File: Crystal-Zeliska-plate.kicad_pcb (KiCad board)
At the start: 2 copper layers, 182.6 x 114.3 mm, 0 parts

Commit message: updated Gerber
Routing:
- net (no net): track 0.00 -> 19.8 mm
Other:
- outline, holes or cut-outs redrawn

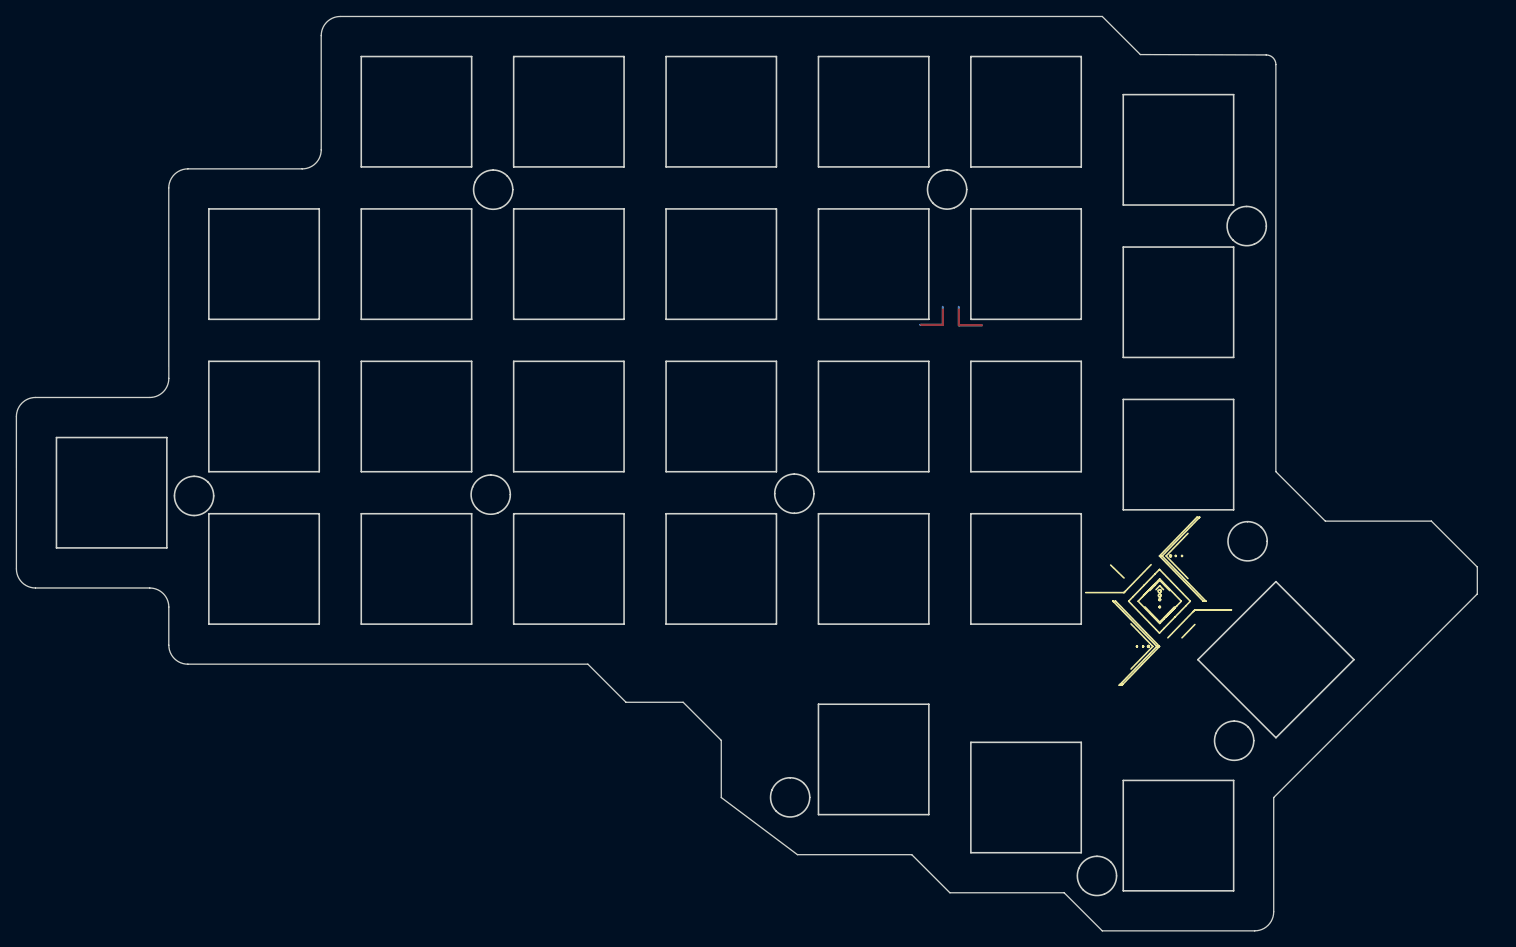
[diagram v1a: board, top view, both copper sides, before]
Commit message: updated PCb with m2.2mm screws
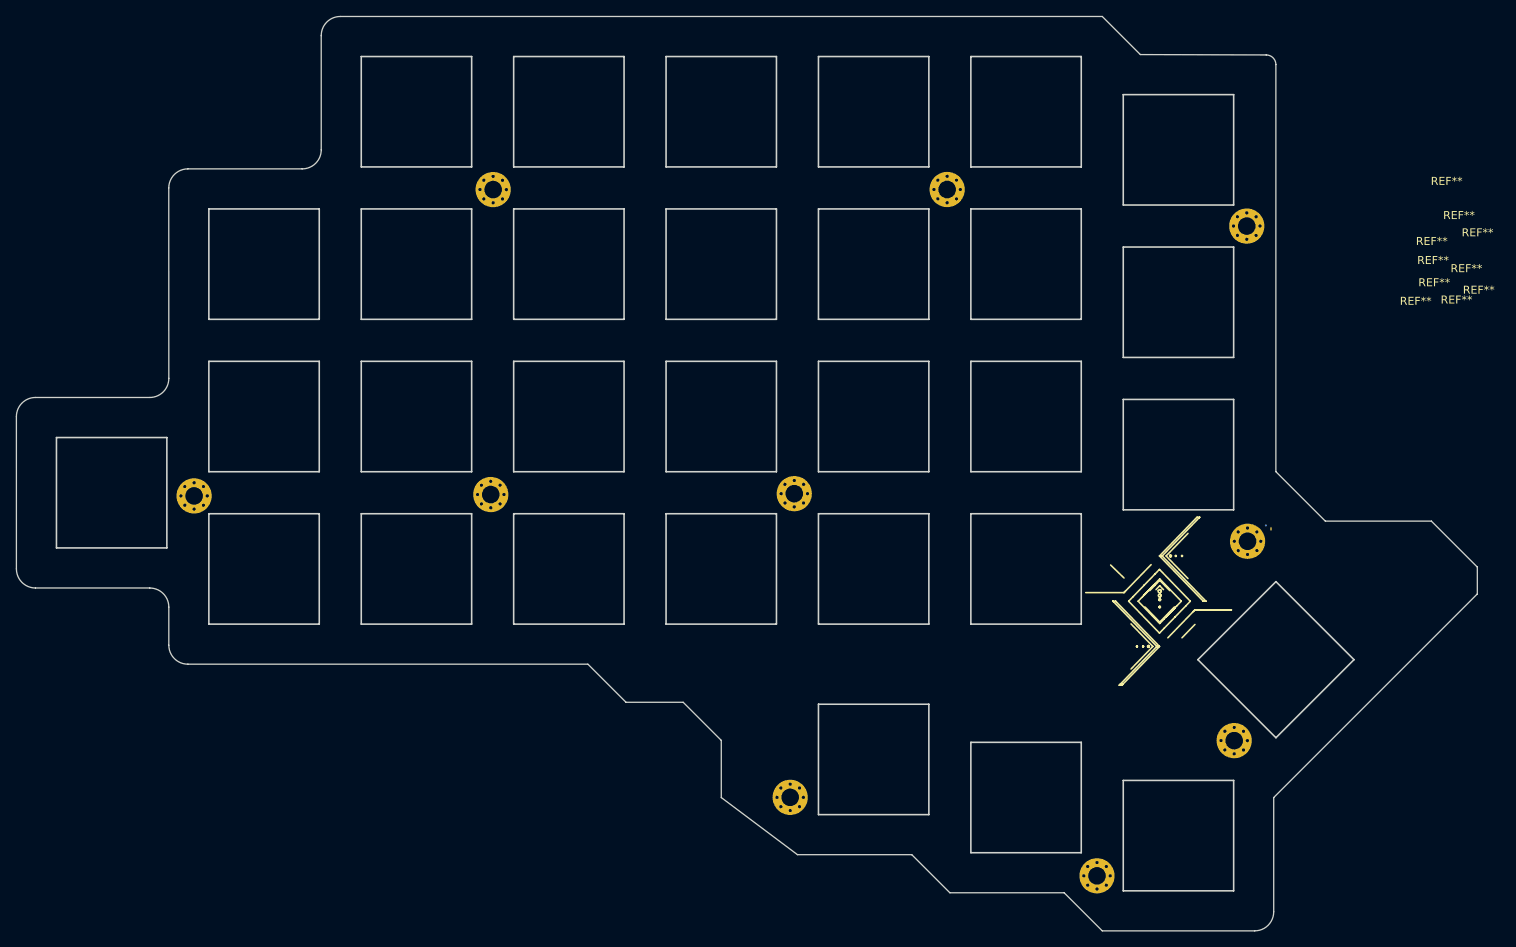
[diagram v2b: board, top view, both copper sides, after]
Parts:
- added REF**: MountingHole_2.2mm_M2_Pad_Via, MountingHole:MountingHole_2.2mm_M2_Pad_Via, F.Cu at (177.3, 142.3)
- added REF**: MountingHole_2.2mm_M2_Pad_Via, MountingHole:MountingHole_2.2mm_M2_Pad_Via, F.Cu at (194.5, 125.4)
- added REF**: MountingHole_2.2mm_M2_Pad_Via, MountingHole:MountingHole_2.2mm_M2_Pad_Via, F.Cu at (139.5, 94.5)
- added REF**: MountingHole_2.2mm_M2_Pad_Via, MountingHole:MountingHole_2.2mm_M2_Pad_Via, F.Cu at (196.0, 61.1)
- added REF**: MountingHole_2.2mm_M2_Pad_Via, MountingHole:MountingHole_2.2mm_M2_Pad_Via, F.Cu at (196.1, 100.5)
- added REF**: MountingHole_2.2mm_M2_Pad_Via, MountingHole:MountingHole_2.2mm_M2_Pad_Via, F.Cu at (101.5, 94.7)
- added REF**: MountingHole_2.2mm_M2_Pad_Via, MountingHole:MountingHole_2.2mm_M2_Pad_Via, F.Cu at (64.5, 94.8)
- added REF**: MountingHole_2.2mm_M2_Pad_Via, MountingHole:MountingHole_2.2mm_M2_Pad_Via, F.Cu at (101.8, 56.5)
- added REF**: MountingHole_2.2mm_M2_Pad_Via, MountingHole:MountingHole_2.2mm_M2_Pad_Via, F.Cu at (158.6, 56.5)
- added REF**: MountingHole_2.2mm_M2_Pad_Via, MountingHole:MountingHole_2.2mm_M2_Pad_Via, F.Cu at (139.0, 132.5)
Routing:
- net (no net): track 19.8 -> 0.27 mm
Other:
- outline, holes or cut-outs redrawn
